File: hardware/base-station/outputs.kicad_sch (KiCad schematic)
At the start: 5 parts, among them J6 Conn_01x04, U6 S25FL256LAGNFI010

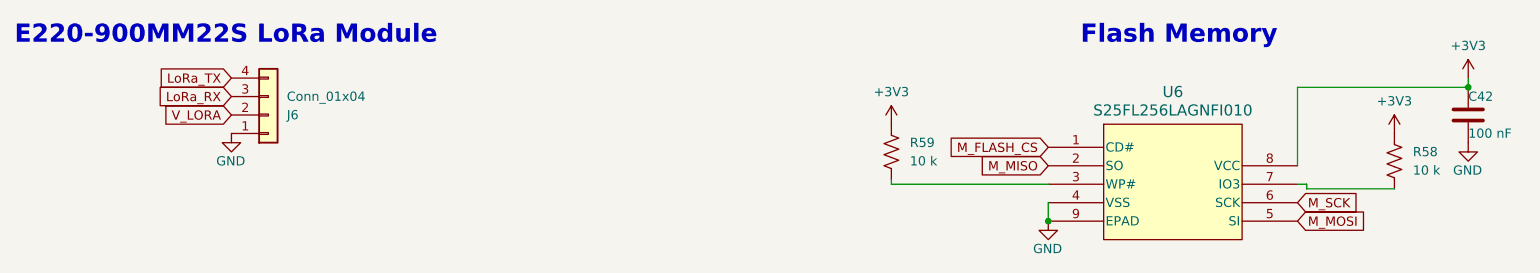
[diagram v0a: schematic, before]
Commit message: hardware: BOM-cost pass across all four boards
Component changes from a cross-board cost review. Per-board component cost
(USD @~100qty): rocket $86.21 -> $61.39, base station $35.91 -> $29.89, with
the LoRa daughterboard and GNSS SAM-M10Q board added to the shared BOM.

Memory architecture
  - Rocket: MR25H10 MRAM deleted; the log ring moves to in-package PSRAM.
    ESP32-S3 -> ESP32-S3RH2 (2 MB quad PSRAM, no in-package flash, same land
    pattern; SPICS1/GPIO26 was already unconnected on every board).
    Persistence across boots is knowingly given up.
  - Rocket NAND F35SQB004G-WWT -> GD5F2GQ5UEYIGR: pin- and footprint-identical
    (verified against the U11 land pattern), 4 Gbit -> 2 Gbit, $11.61 -> $3.50.
    Needs the 4096 -> 2048 B page migration in firmware.
  - Base station: dedicated log flash deleted entirely. It wrote one ~183 B CSV
    row per received packet at the 2 Hz downlink (~366 B/s, and only while a
    flight is active), so 256 MB was ~204 hours of headroom. The firmware
    already falls back to the existing SPIFFS partition, so this promotes a
    tested path rather than needing new code.
  - Boot flash W25Q64JVXGIQ -> W25Q128JVSIQ on all four positions: 16 MB for
    LESS money ($3.10 -> $2.21). SCHEMATIC ONLY - the boards still need
    "Update PCB from Schematic" plus re-placement, since SOIC-8 208mil is 2.2x
    the DFN's area. The DFN's 9th (exposed) pad was a redundant GND tie; pin 4
    is GND on all four, so nothing is lost.

Power
  - LoRa + GNSS keep TPS62913 (low-noise, RF rails). The rocket briefly moved
    to it and was REVERTED to TPS62152: the TPS62913 is forced-PWM with 5 mA
    quiescent, which would have raised the pad-idle floor ~6x against the
    light-sleep work.
  - Base load switch TPS22810 -> TPS22918 (identical footprint and pin order;
    pin 3 EN/UVLO -> ON is safe because it was driven as a plain enable).
    CT cap 10 nF -> 2.2 nF to match the rocket's ramp; R8 (QOD->VOUT) deleted.
  - LoRa gains a 7.5k S-CONF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
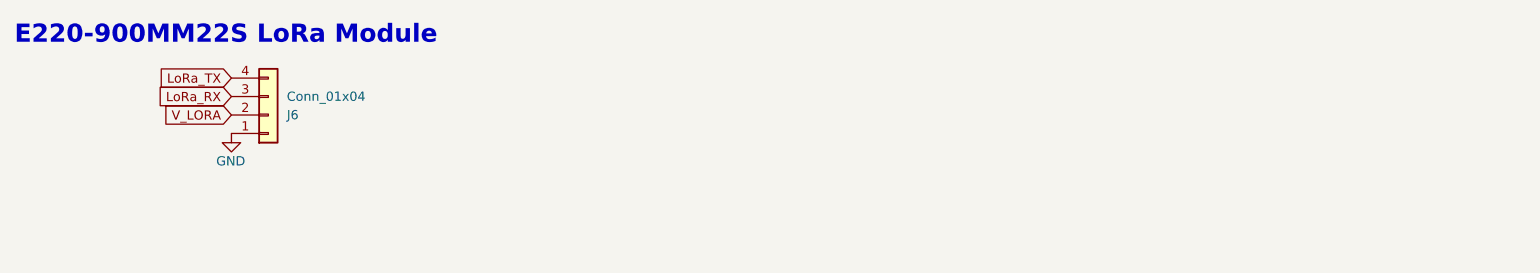
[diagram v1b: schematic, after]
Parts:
- removed C42: 100 nF, Capacitor_SMD:C_0402_1005Metric, symbol Device:C
- removed R58, R59: 10 k, Resistor_SMD:R_0402_1005Metric, symbol Device:R_US
- removed U6: S25FL256LAGNFI010, S25FL256LAGNFI010_CYP, symbol Custom:S25FL256LAGNFI010
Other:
- note removed: "Flash Memory"

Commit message: hardware: battery protection, boost swap, and a capacitor voltage audit
Base station power chain, all verified against exported netlists:

- Protection: MAX17303G+ gauge/protector and its NTMD6N02R2G FET pair
  replaced by DW01A + 2x FS8205A. The MAX17303 had no firmware driver and
  the board never had a working coulomb counter, so state of charge already
  came from the voltage curve in bs_battery_soc.h; it now reads a 1M/1M
  divider on GPIO1. The FETs move from the positive rail to the negative
  one because the DW01A has no charge pump, so board ground is now P-,
  separated from the cell's B- by the FET stack. Two FS8205A in parallel
  put the 150 mV overcurrent trip at ~4.8-6.0 A instead of ~2.4-3.0 A.
  TH1 moves onto the BQ21040's TS pin, replacing a fixed 10k that had been
  defeating thermal charge cutoff.

- V_LORA retargeted 7.49 V -> 4.95 V and LM5157QRTERQ1 -> TPS61023DRLR.
  Nothing needed 7.4 V (everything downstream is 3.3 V behind the
  TPS62913), while an RFD868x-class radio is 5 V nominal with a 6 V
  absolute maximum, so the old rail put it permanently out of reach. Being
  synchronous and internally compensated also dropped D2, C35-C38 and R10.
  Inductor stays the fleet 2.2 uH: inside TI's 0.37-2.9 uH range and the
  only value meeting their ripple-under-40%-of-average guidance at load.

- Keystone 1043P holder -> MYOUNG BH-18650-A5BJ001-2D. Terminal pitch
  72.30 vs 72.22 mm, so the battery nets did not move; BT2 is rotated 180
  degrees because this part's positive end is mirrored.

Across all four boards:

- Every crystal was mis-loaded. 32.768 kHz parts saw ~9 pF against a 6 pF
  spec and the 40 MHz saw 12.5 pF against 10 pF, both pulling slow. Moved
  to Seiko SC-32S (12.5 pF) with 22 pF load caps, and the 40 MHz caps to
  18 pF. The tolerance being paid for had been swamped several times over.

- Capacitor voltage audit, new Min V rating column in the BOM. Three parts
  were operating outside their rating on 8.4 V rails: 47 uF and 100 u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
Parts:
- removed J6: Conn_01x04, Connector_JST:JST_SH_BM04B-SRSS-TB_1x04-1MP_P1.00mm_Vertical, symbol Connector_Generic:Conn_01x04
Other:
- note removed: "E220-900MM22S LoRa Module"
